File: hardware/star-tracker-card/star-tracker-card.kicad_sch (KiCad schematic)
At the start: 8 parts, among them J1 SM14B-SHLS-TF, J101 3-1734592-64-1734592-0, J4 TFM-120-01-L-D-RA, J7 GRPB041VWVN-RC

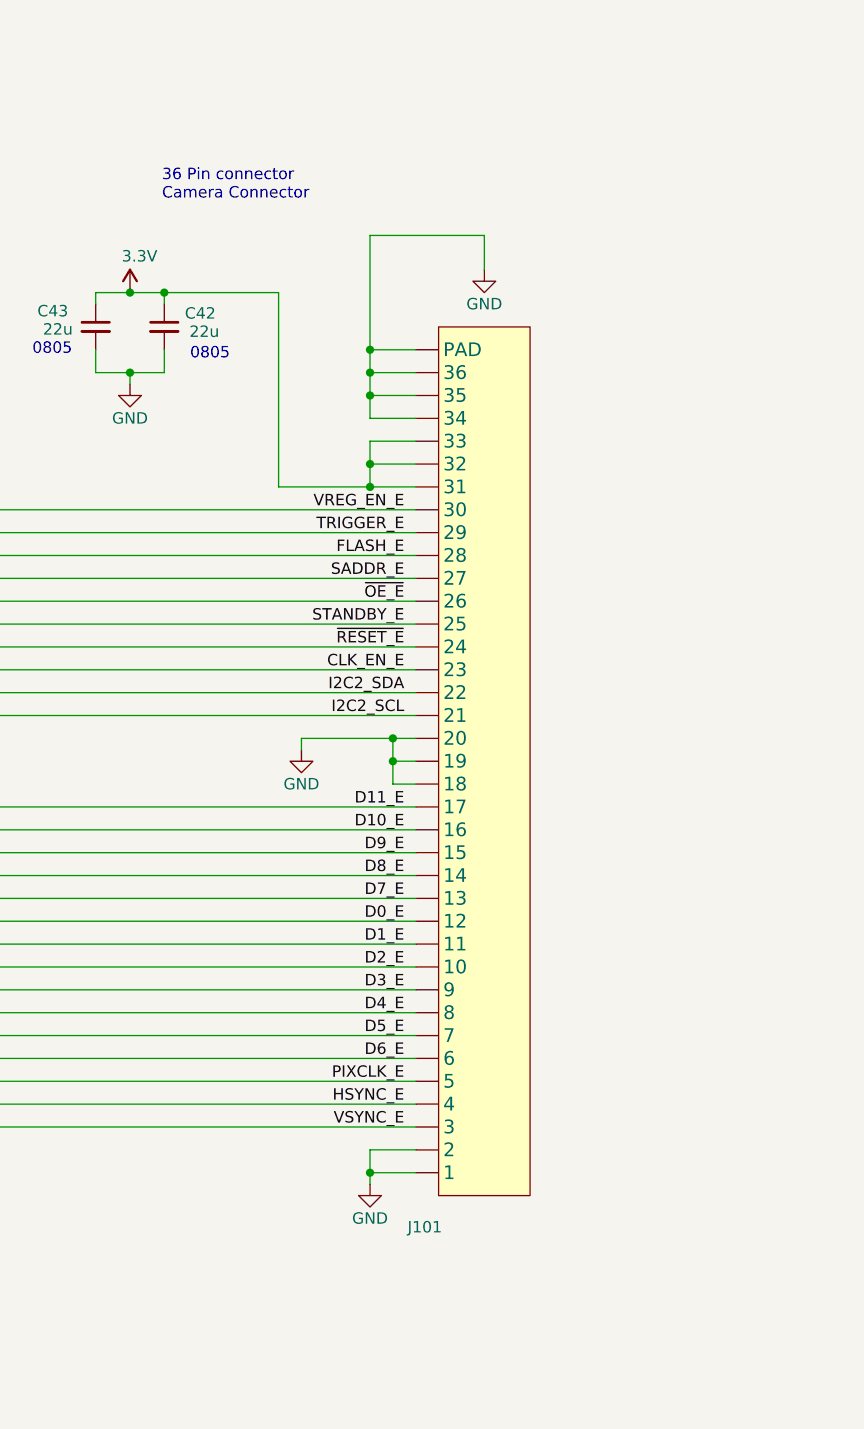
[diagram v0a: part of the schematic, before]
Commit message: Added FFC cable part number
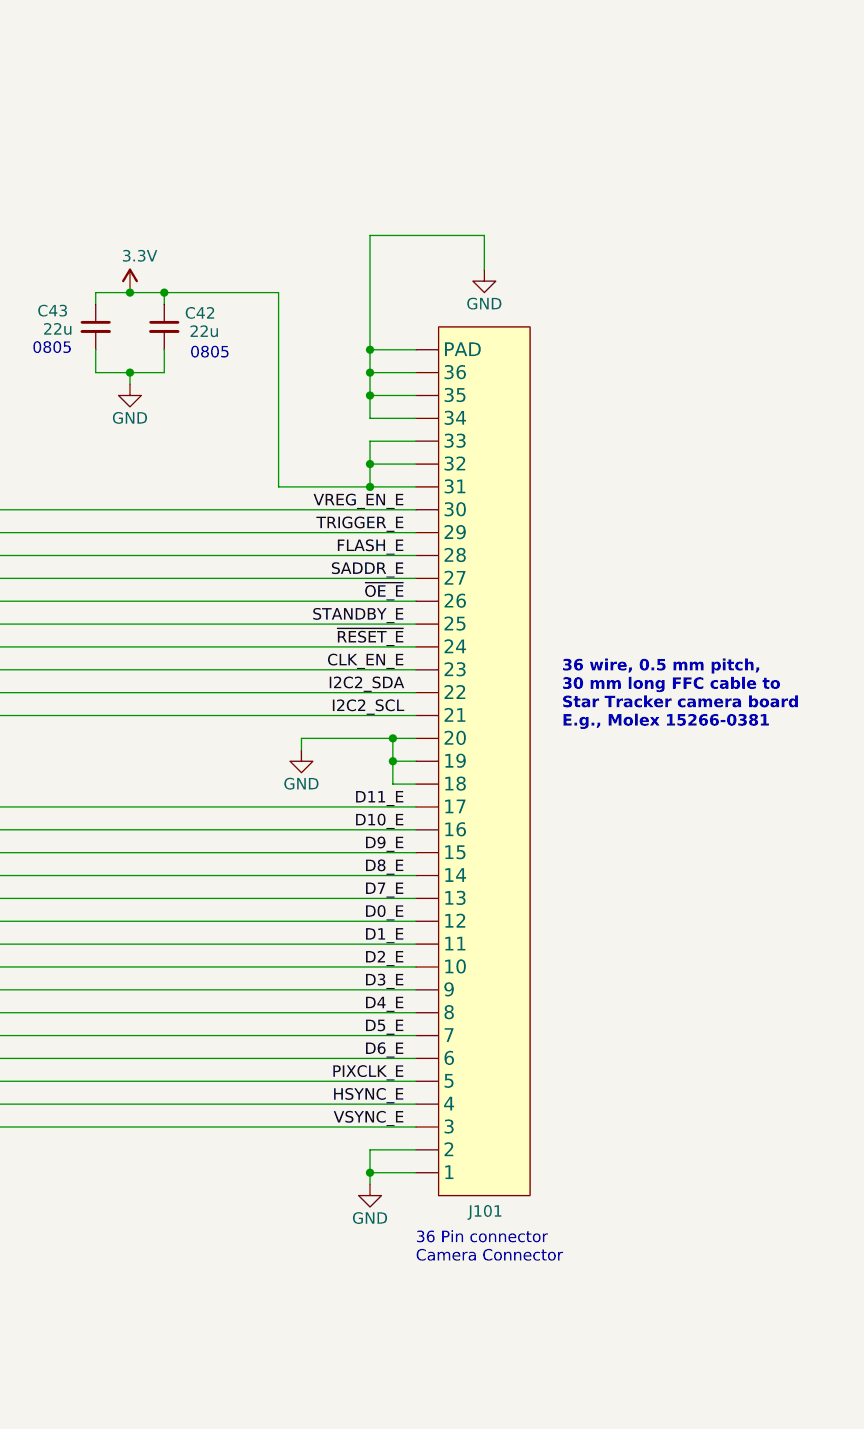
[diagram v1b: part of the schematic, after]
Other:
- note added: "36 wire, 0.5 mm pitch, 30 mm long FFC cable to Star Tracker camera board E.g., Molex 15266-0381"
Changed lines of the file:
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@@
 		)
 	)
+	(text "36 wire, 0.5 mm pitch, \n30 mm long FFC cable to\nStar Tracker camera board\nE.g., Molex 15266-0381\n"
+		(exclude_from_sim no)
+		(at 382.016 142.494 0)
+		(effects
+			(font
+				(size 1.27 1.27)
+				(thickness 0.254)
+				(bold yes)
+			)
+			(justify left)
+		)
+	)
 	(text "Main Connector"
 		(exclude_from_sim no)
@@
 	(text "36 Pin connector\nCamera Connector"
 		(exclude_from_sim no)
-		(at 337.566 87.63 0)
+		(at 365.76 205.74 0)
 		(effects
 			(font
@@
 		(dnp no)
 		(property "Reference" "J101"
-			(at 364.8456 200.8886 0)
+			(at 371.602 199.136 0)
 			(show_name no)
 			(do_not_autoplace no)
